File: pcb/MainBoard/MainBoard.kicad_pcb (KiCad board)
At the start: 4 copper layers, 50 x 50 mm, 133 parts, among them J101 Conn_02x05_Odd_Even, J301 USB_C_Receptacle_USB2.0, J501 Conn_01x01, J502 Conn_01x01, J503 Conn_01x01, J504 Conn_01x01, J505 Conn_01x01, J506 Conn_01x01, J507 Conn_01x01, J508 Conn_01x01, J509 Conn_01x01, J510 Conn_01x01, J511 Conn_01x01, J512 Conn_01x01, J513 Conn_01x01, J514 Conn_01x01, J515 Conn_01x01, J516 Conn_01x01, J517 Conn_01x01, J518 Conn_01x01, J519 Conn_01x01, J520 Conn_01x01, J801 AudioJack3_Ground, Q501 HL2304, U201 SHOU HAN TF PUSH, U401 RP2040, U402 W25Q128JVSIQ, U601 TJA1050T, U701 XC6206PxxxMR-Regulator_Linear, U702 INA180A1, X401 12MHz

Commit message: dump pcb
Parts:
- removed C406: 100nF, Capacitor_SMD:C_0402_1005Metric
- removed C704: 100u, Capacitor_Tantalum_SMD:CP_EIA-3528-15_AVX-H
- removed TP704: TestPoint, TestPoint:TestPoint_Pad_D1.0mm
- added C105: 22u, Capacitor_SMD:C_0805_2012Metric, F.Cu at (157.5, 34.7)
- added C106: 22u, Capacitor_SMD:C_0805_2012Metric, F.Cu at (160.6, 36.8)
- added C501: 22u, Capacitor_SMD:C_0805_2012Metric, F.Cu at (147.6, 33.5)
- added C502: 470u, Capacitor_SMD:CP_Elec_8x10.5, F.Cu at (123.7, 45.9)
- added C503: 100u, Capacitor_Tantalum_SMD:CP_EIA-3528-15_AVX-H, F.Cu at (126.2, 37.7)
- added C504: 22u, Capacitor_SMD:C_0805_2012Metric, F.Cu at (124.2, 55.1)
- added C505: 22u, Capacitor_SMD:C_0805_2012Metric, F.Cu at (137.0, 58.5)
- added C709: 4.7uF, Capacitor_SMD:C_0805_2012Metric, F.Cu at (142.3, 60.4)
- added C710: 4.7uF, Capacitor_SMD:C_0805_2012Metric, F.Cu at (139.6, 57.4)
- added C711: 4.7uF, Capacitor_SMD:C_0603_1608Metric, F.Cu at (147.0, 54.9)
- added C712: 4.7uF, Capacitor_SMD:C_0805_2012Metric, F.Cu at (139.6, 53.6)
- added C713: 100u, Capacitor_SMD:C_1206_3216Metric, F.Cu at (154.5, 52.6)
- added C714: 100pF, Capacitor_SMD:C_0402_1005Metric, F.Cu at (137.7, 66.5)
- added H501: JLCToolingHole, led-matrix:jlcpcb-tooling-hole, F.Cu at (167.5, 33.5)
- added H502: JLCToolingHole, led-matrix:jlcpcb-tooling-hole, F.Cu at (167.5, 81.0)
- added H503: JLCToolingHole, led-matrix:jlcpcb-tooling-hole, F.Cu at (120.0, 33.5)
- added H504: JLCToolingHole, led-matrix:jlcpcb-tooling-hole, F.Cu at (120.0, 81.0)
- added J102: Mechanical, Connector_PinHeader_2.54mm:PinHeader_1x02_P2.54mm_Vertical, F.Cu at (158.7, 69.8)
- added J103: Mechanical, Connector_PinHeader_2.54mm:PinHeader_1x02_P2.54mm_Vertical, F.Cu at (127.5, 34.2)
- added J104: Mechanical, Connector_PinHeader_2.54mm:PinHeader_1x02_P2.54mm_Vertical, F.Cu at (120.8, 73.5)
- added J105: DebugConn, Connector_PinSocket_2.54mm:PinSocket_1x05_P2.54mm_Horizontal, B.Cu at (158.6, 49.5)
- added J601: CANConn, Connector_JST:JST_EH_S2B-EH_1x02_P2.50mm_Horizontal, F.Cu at (157.5, 75.4)
- added JP101: SolderJumper_3_Open, led-matrix:SolderJumper-3_Open_RoundedPad_Smol, B.Cu at (159.7, 41.5)
- added JP102: SolderJumper_3_Open, led-matrix:SolderJumper-3_Open_RoundedPad_Smol, B.Cu at (159.8, 38.0)
- added JP103: SolderJumper_3_Open, led-matrix:SolderJumper-3_Open_RoundedPad_Smol, F.Cu at (148.4, 35.3)
- added JP104: SolderJumper_3_Open, led-matrix:SolderJumper-3_Open_RoundedPad_Smol, B.Cu at (134.6, 36.9)
- added JP504: SolderJumper_3_Open, led-matrix:SolderJumper-3_Open_RoundedPad_Smol, F.Cu at (162.2, 34.0)
- added JP505: SolderJumper_3_Open, led-matrix:SolderJumper-3_Open_RoundedPad_Smol, B.Cu at (125.4, 61.2)
- added JP506: SolderJumper_3_Open, led-matrix:SolderJumper-3_Open_RoundedPad_Smol, B.Cu at (132.2, 61.2)
- added JP507: SolderJumper_3_Open, led-matrix:SolderJumper-3_Open_RoundedPad_Smol, B.Cu at (128.5, 57.0)
- added JP508: SolderJumper_3_Open, led-matrix:SolderJumper-3_Open_RoundedPad_Smol, B.Cu at (128.4, 65.1)
- added JP509: SolderJumper_3_Open, led-matrix:SolderJumper-3_Open_RoundedPad_Smol, B.Cu at (129.5, 66.8)
- added JP601: SolderJumper_2_Open, led-matrix:SolderJumper-2_Open_RoundedPad_Smol, B.Cu at (156.2, 71.5)
- added JP701: SolderJumper_3_Open, led-matrix:SolderJumper-3_Open_RoundedPad_Smol, B.Cu at (139.5, 55.5)
- added Q502: HL2304, Package_TO_SOT_SMD:SOT-23, F.Cu at (128.8, 61.1)
- added Q503: HL2304, Package_TO_SOT_SMD:SOT-23, F.Cu at (125.4, 61.1)
- added Q504: HL2304, Package_TO_SOT_SMD:SOT-23, F.Cu at (132.2, 61.1)
- added Q505: HL2304, Package_TO_SOT_SMD:SOT-23, F.Cu at (127.2, 56.0)
- added Q506: HL2304, Package_TO_SOT_SMD:SOT-23, F.Cu at (126.1, 65.8)
- added Q507: HL2304, Package_TO_SOT_SMD:SOT-23, F.Cu at (130.9, 65.9)
- added R105: 2k2, Resistor_SMD:R_0402_1005Metric, F.Cu at (136.0, 39.1)
- added R106: 2k2, Resistor_SMD:R_0402_1005Metric, F.Cu at (137.1, 38.7)
- added R213: 47k, Resistor_SMD:R_0603_1608Metric, F.Cu at (147.1, 72.4)
- added R214: 47k, Resistor_SMD:R_0603_1608Metric, F.Cu at (145.6, 72.4)
- added R215: 47k, Resistor_SMD:R_0603_1608Metric, F.Cu at (144.1, 72.4)
- added R216: 47k, Resistor_SMD:R_0603_1608Metric, F.Cu at (142.6, 72.4)
- added R508: 4k7, Resistor_SMD:R_0402_1005Metric, F.Cu at (128.3, 58.7)
- added R509: 10k, Resistor_SMD:R_0402_1005Metric, F.Cu at (128.9, 63.5)
- added R510: 4k7, Resistor_SMD:R_0402_1005Metric, F.Cu at (131.7, 58.7)
- added R511: 10k, Resistor_SMD:R_0402_1005Metric, F.Cu at (132.2, 63.5)
- added R512: 4k7, Resistor_SMD:R_0402_1005Metric, F.Cu at (134.4, 56.6)
- added R513: 4k7, Resistor_SMD:R_0402_1005Metric, F.Cu at (123.7, 66.4)
- added R514: 10k, Resistor_SMD:R_0402_1005Metric, F.Cu at (128.5, 66.3)
- added R515: 4k7, Resistor_SMD:R_0402_1005Metric, F.Cu at (133.8, 65.9)
- added R602: 120R, Resistor_SMD:R_0402_1005Metric, F.Cu at (156.2, 71.5)
- added R705: 1k5, Resistor_SMD:R_0402_1005Metric, F.Cu at (139.0, 61.4)
- added R706: 470R, Resistor_SMD:R_0402_1005Metric, F.Cu at (145.0, 55.1)
- added R707: 1k, Resistor_SMD:R_0402_1005Metric, F.Cu at (145.0, 53.2)
- added R708: 1k8, Resistor_SMD:R_0402_1005Metric, F.Cu at (146.0, 53.2)
- added R709: 150R, Resistor_SMD:R_0402_1005Metric, F.Cu at (147.0, 53.2)
- added SW101: SW, Button_Switch_SMD:SW_SPST_B3U-3000P, F.Cu at (166.5, 56.2)
- added SW102: SW, Button_Switch_SMD:SW_SPST_B3U-3000P, F.Cu at (166.5, 51.2)
- added TP706: TestPoint, TestPoint:TestPoint_Pad_D1.0mm, B.Cu at (139.5, 57.9)
- added TP707: TestPoint, TestPoint:TestPoint_Pad_D1.0mm, B.Cu at (139.5, 53.1)
- added U703: XC6206PxxxMR-Regulator_Linear, Package_TO_SOT_SMD:SOT-23, F.Cu at (142.3, 57.4)
- added U704: CJ431, Package_TO_SOT_SMD:SOT-23, F.Cu at (142.5, 53.7)
- C101, C102, C103, C104: value C -> 1uf; footprint Capacitor_SMD:C_0603_1608Metric -> Capacitor_SMD:C_0402_1005Metric
- C703: value 4.7uF -> 22u
- C705: value 22uF -> 100u; footprint Capacitor_SMD:C_1206_3216Metric -> Capacitor_SMD:CP_Elec_6.3x7.7
- C706, C708: value 22uF -> 22u; footprint Capacitor_SMD:C_1206_3216Metric -> Capacitor_SMD:C_0805_2012Metric
- J101: value Conn_02x05_Odd_Even -> DaughterConn; footprint Connector_PinHeader_2.00mm:PinHeader_2x05_P2.00mm_Vertical -> Connector_PinHeader_2.54mm:PinHeader_2x05_P2.54mm_Vertical
- J501, J502, J503, J504, J505, J506, J507, J508, J509, J510, J511, J512, J513, J514, J515, J516, J517, J518, J519, J520, U201: moved to B.Cu
- JP501, JP502: value SolderJumper_2_Open -> SolderJumper_3_Open; footprint Jumper:SolderJumper-2_P1.3mm_Open_RoundedPad1.0x1.5mm -> led-matrix:SolderJumper-3_Open_RoundedPad_Smol; moved to B.Cu
- JP503: footprint Jumper:SolderJumper-3_P1.3mm_Open_RoundedPad1.0x1.5mm -> led-matrix:SolderJumper-3_Open_RoundedPad_Smol; moved to B.Cu
- Q501: footprint PCM_Package_TO_SOT_SMD_AKL:SOT-23 -> Package_TO_SOT_SMD:SOT-23
- R103, R104: value 100R -> 4k7
- R201, R202, R203, R204, R205, R206, R211, R212: value 10k -> 47k
- R207, R208, R209, R210: value 10k -> 33R; footprint Resistor_SMD:R_0603_1608Metric -> Resistor_SMD:R_0402_1005Metric
- R501, R507: value 10k -> 4k7
- U701: value XC6206PxxxMR-Regulator_Linear -> AMS1117-3.3; footprint Package_TO_SOT_SMD:SOT-23 -> Package_TO_SOT_SMD:SOT-223-3_TabPin2
- moved R601 141.3 mm to (152.3, 61.1), turned to 90 degrees
- moved R503 141.1 mm to (159.8, 34.5), turned to -90 degrees
- moved C601 139.6 mm to (153.3, 61.1), turned to 90 degrees
- moved U601 136.1 mm to (154.0, 65.8), turned to -90 degrees
- moved D601 136.0 mm to (158.0, 72.2)
- moved D602 133.9 mm to (154.5, 72.2), turned to 180 degrees
- moved R502 132.9 mm to (151.3, 35.0), turned to 180 degrees
- moved D501 131.1 mm to (164.8, 33.8)
- moved J510 128.3 mm to (163.5, 32.2)
- moved J509 128.2 mm to (161.2, 32.2)
- moved C706 126.1 mm to (147.2, 80.8), turned to 0 degrees
- moved C708 121.8 mm to (135.6, 80.8), turned to 180 degrees
- moved TP702 120.0 mm to (136.2, 75.8)
- moved C705 119.5 mm to (141.6, 78.4), turned to 0 degrees
- moved TP703 117.4 mm to (134.8, 72.4)
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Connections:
- net Net-(J301-SHIELD) renamed /usbc/USB_SHIELD
- C101 pad 1: /CC1 -> /CC1_F
- C102 pad 1: /CC2 -> /CC2_F
- C103 pad 1: GND -> /5v_sense_F
- C104 pad 1: /Isense -> /Isense_F
- C701 pad 1: /power/5V_FILTERED -> +5V
- C708 pad 1: +5V -> /power/VBUS
- D505 pad 1: /COL_SER -> /pads/COL_SER_OUT
- D506 pad 1: /COL_~{OE} -> /pads/COL_~{OE}_OUT
- D507 pad 1: /COL_RCLK -> /pads/COL_RCLK_OUT
- D508 pad 1: /COL_SRCLK -> /pads/COL_SRCLK_OUT
- D509 pad 1: /COL_~{SRCLR} -> /pads/COL_~{SRCLR}_OUT
- J101 pad 1: /GPIO15 -> +5V
- J101 pad 2: +5V -> +3V3
- J101 pad 3: /GPIO14 -> /GPIO15
- J101 pad 4: +3V3 -> /GPIO14
- J101 pad 6: /GPIO9 -> /GPIO12
- J101 pad 7: /GPIO12 -> /GPIO11
- J101 pad 9: /GPIO11 -> /GPIO9
- JP501 pad 1: /pads/COL_VCC -> +3V3
- JP501 pad 2: +3V3 -> /pads/COL_VCC
- JP502 pad 1: /pads/COL_VCC -> /COL_RCLK
- JP502 pad 2: +5V -> /pads/COL_RCLK_OUT
- JP503 pad 1: /COL_SER -> /pads/COL_SER_5V_BIDI
- JP503 pad 2: /pads/COL_SER_OUT -> Net-(JP503-C)
- Q501 pad 3: /pads/COL_SER_5V -> /pads/COL_SER_5V_BIDI
- R101 pad 2: Net-(R101-Pad2) -> /RESET_SW
- R102 pad 2: Net-(R102-Pad2) -> /CS_SW
- R202 pad 2: /SD_MISO -> /microsd/SD_MISO_DAT0
- R203 pad 2: /SD_SCLK -> /microsd/SD_CLK
- R204 pad 2: /SD_MOSI -> /microsd/SD_MOSI_CMD
- R205 pad 2: /SD_CS -> /microsd/SD_CS_DAT3
- R207 pad 1: /microsd/SD_DAT1 -> /SD_CS
- R207 pad 2: GND -> /microsd/SD_CS_DAT3
- R208 pad 1: /SD_MISO -> /SD_MOSI
- R208 pad 2: GND -> /microsd/SD_MOSI_CMD
- R209 pad 2: GND -> /microsd/SD_CLK
- R210 pad 1: /SD_MOSI -> /SD_MISO
- R210 pad 2: GND -> /microsd/SD_MISO_DAT0
- R211 pad 1: /SD_CS -> /microsd/SD_DAT1
- R212 pad 1: /microsd/SD_DAT2 -> /microsd/SD_MISO_DAT0
- R402 pad 1: /USB_D- -> /USB_D+
- R403 pad 1: /USB_D+ -> /USB_D-
- R501 pad 1: /pads/COL_VCC -> +5V
- R501 pad 2: /COL_~{OE} -> /pads/COL_~{OE}_5V
- R503 pad 1: /pads/ROW_VLED -> Net-(JP504-B)
- R504 pad 1: /COL_~{SRCLR} -> /COL_~{OE}
- R701 pad 2: GND -> /5V_sense
- U201 pad 2: /SD_CS -> /microsd/SD_CS_DAT3
- U201 pad 3: /SD_MOSI -> /microsd/SD_MOSI_CMD
- U201 pad 5: /SD_SCLK -> /microsd/SD_CLK
- U201 pad 7: /SD_MISO -> /microsd/SD_MISO_DAT0
- U401 pad 14: /GPIO13 -> /GPIO11
- U401 pad 16: /GPIO11 -> /GPIO13
- U401 pad 17: /ROW_SER -> /rp2040/GPIO14
- U401 pad 18: /ROW_~{SRCLR} -> /rp2040/GPIO15
- U401 pad 24: /rp2040/SWCLK -> /SWCLK
- U401 pad 25: /rp2040/SWD -> /SWD
- U401 pad 29: /ROW_~{OE} -> /ROW_SRCLK
- U401 pad 30: /ROW_RCLK -> /ROW_~{OE}
- U401 pad 31: /ROW_SRCLK -> /ROW_RCLK
- U401 pad 40: GND -> /5v_sense_F
- U401 pad 41: /Isense -> /Isense_F
- U401 pad 7: /CAN_TXD -> /CAN_RXD
- U401 pad 8: /CAN_RXD -> /CAN_S
- U401 pad 9: /CAN_S -> /CAN_TXD
- U701 pad 3: /power/5V_FILTERED -> +5V
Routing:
- net GND: track 0.00 -> 212.6 mm, vias 0 -> 217
- net +3V3: track 0.00 -> 188.9 mm, vias 0 -> 16
- net +5V: track 0.00 -> 176.2 mm, vias 0 -> 19
- net /COL_~{OE}: track 0.00 -> 59.2 mm, vias 0 -> 2
- net /COL_~{SRCLR}: track 0.00 -> 57.1 mm, vias 0 -> 4
- net /COL_RCLK: track 0.00 -> 54.6 mm, vias 0 -> 2
- net /COL_SRCLK: track 0.00 -> 50.5 mm, vias 0 -> 2
- net /COL_SER: track 0.00 -> 50.5 mm, vias 0 -> 2
- net /CC1: track 0.00 -> 47.1 mm, vias 0 -> 2
- net /microsd/SD_CS_DAT3: track 0.00 -> 45.0 mm, vias 0 -> 4
- net /microsd/SD_CLK: track 0.00 -> 44.8 mm, vias 0 -> 2
- net /CC2: track 0.00 -> 42.0 mm, vias 0 -> 2
- net /microsd/SD_MOSI_CMD: track 0.00 -> 41.9 mm, vias 0 -> 2
- net /USB_D+: track 0.00 -> 41.6 mm, vias 0 -> 2
- net /USB_D-: track 0.00 -> 38.3 mm, vias 0 -> 2
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- added copper zone on B.Cu, net +3V3
- added copper zone on B.Cu, net +5V
- added copper zone on F.Cu, net +5V
- added copper zone on In1.Cu, net +5V
- added copper zone on F.Cu, net /power/5V_FILTERED
- added copper zone on In1.Cu, net /power/5V_FILTERED
- added copper zone on F.Cu, net /power/VBUS
- added copper zone on B.Cu, net /usbc/USB_SHIELD
- added copper zone on B.Cu, net GND
- added copper zone on F.Cu, net GND
- added copper zone on In1.Cu, net GND
- added copper zone on In2.Cu, net GND
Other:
- board text added: "(le bodge)"
- board text added: "10"
- board text added: "11"
- board text added: "12"
- board text added: "120Ω termination"
- board text added: "13"
- board text added: "14·"
- board text added: "15·"
- board text added: "2024"
- board text added: "3V3"
- board text added: "5V"
- board text added: "5V_F"
- board text added: "9"
- board text added: "AUDIO"
- board text added: "B"
- board text added: "BOOT"
- board text added: "CAN"
- board text added: "COL|SEP."
- board text added: "DEBUG"
- board text added: "GND"
- board text added: "GPIO"
- board text added: "GPIO|SER"
- board text added: "GPIO|~{SRCLR}"
- board text added: "HSWAW"
- board text added: "JLCJLCJLCJLC"
- board text added: "PIN 14"
- board text added: "PIN 15"
- board text added: "R"
- board text added: "RCLK"
- board text added: "RESET"
- board text added: "RX"
- board text added: "Reg."
- board text added: "Rev A"
- board text added: "SEP.|COL"
- board text added: "SER"
- board text added: "SRCLK"
- board text added: "SWC"
- board text added: "SWCLK"
- board text added: "SWD"
- board text added: "Shunt"
- board text added: "TX"
- board text added: "USB"
- board text added: "VBUS"
- board text added: "VCC"
- board text added: "VLED"
- board text added: "Vref"
- board text added: "bidi"
- board text added: "by radex"
- board text added: "column driver level shifting"
- board text added: "le bodge"
- board text added: "main board"
- board text added: "matri"
- board text added: "microSD"
- board text added: "rad"
- board text added: "radex"
- board text added: "x"
- board text added: "~{OE}"
- board text added: "~{SRCLR}"
- board text added: "·14"
- board text added: "·15"

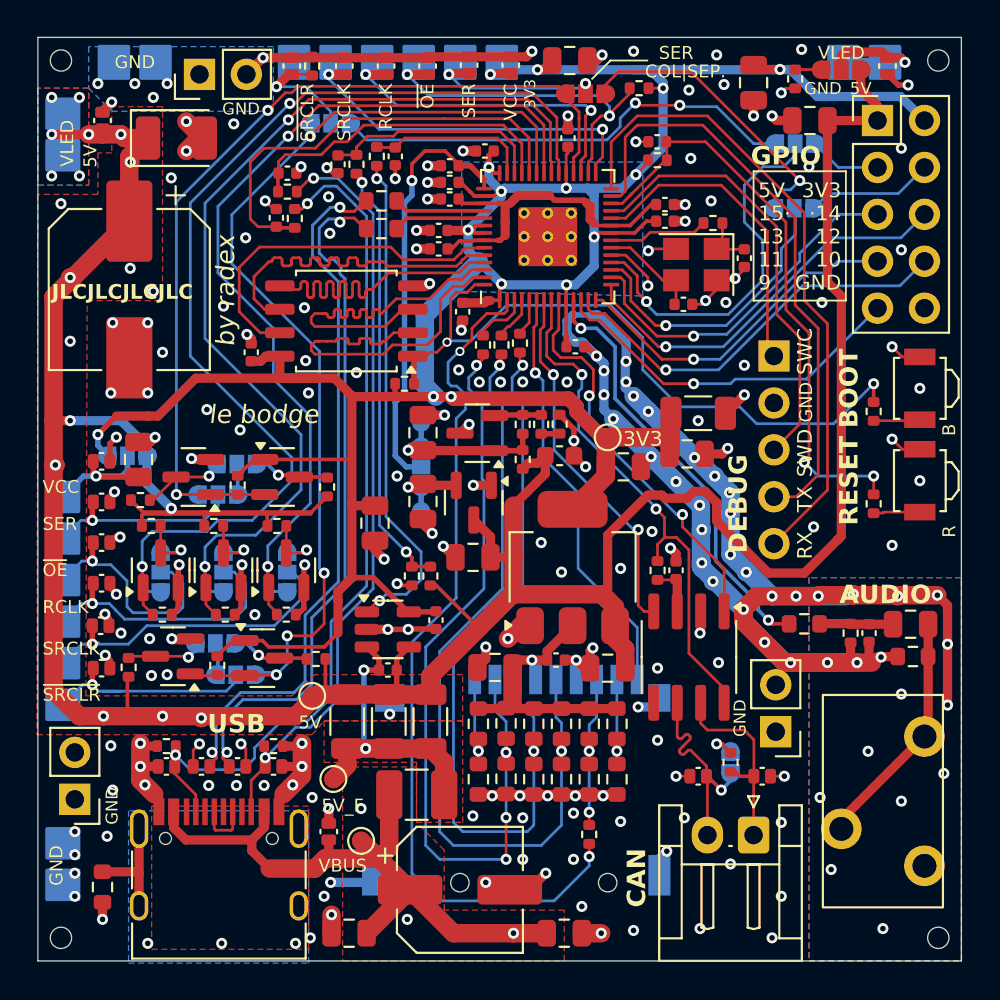
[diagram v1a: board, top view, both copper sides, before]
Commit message: MainBoard: fixes, simplify, BOM optimize, DRC fixes, ERC fixes
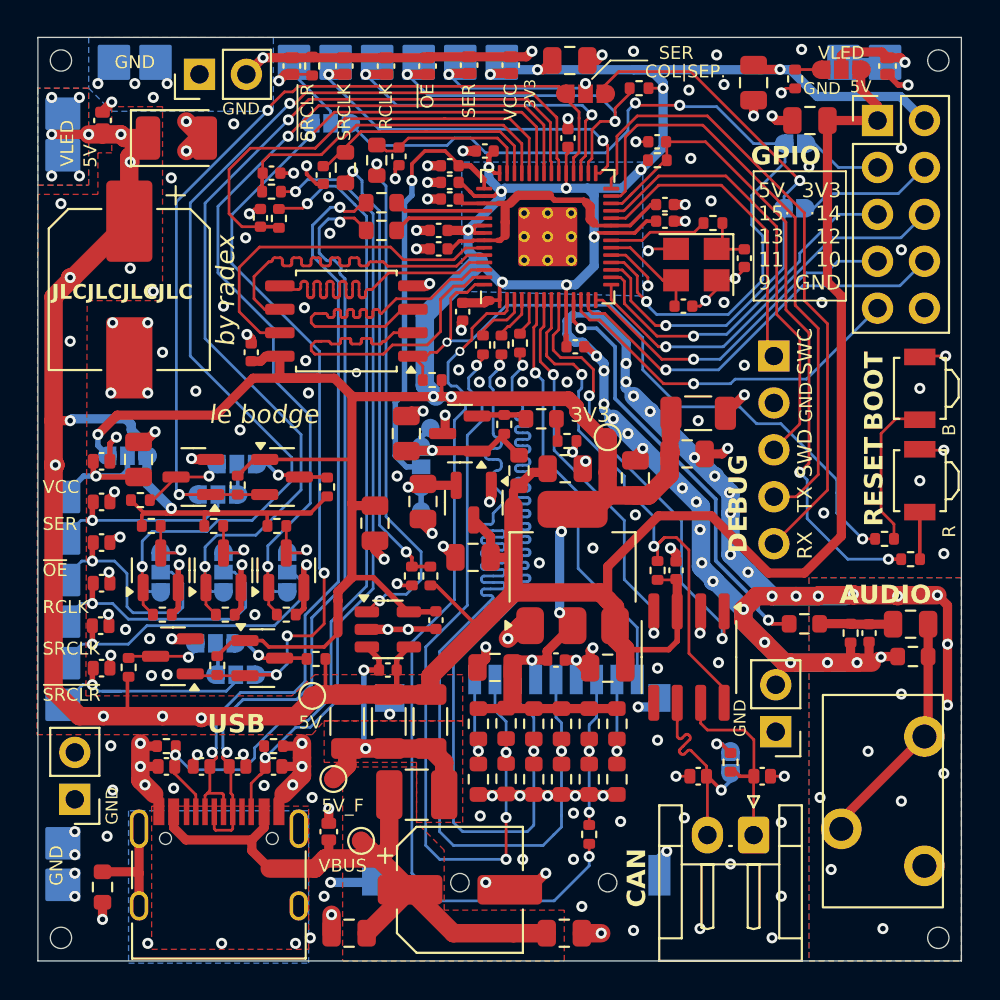
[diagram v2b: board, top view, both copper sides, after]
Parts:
- C101, C102, C103, C104: value 1uf -> 1u
- C401, C402, C403, C404, C405, C407, C408, C409, C410, C416, C707: value 100nF -> 100n
- C411, C412, C413: value 1uF -> 1u
- C414, C415: value 33pF -> 33p
- C701, C702, C709, C710, C712: value 4.7uF -> 4u7
- C711: value 4.7uF -> 4u7; footprint Capacitor_SMD:C_0603_1608Metric -> Capacitor_SMD:C_0805_2012Metric
- C714: value 100pF -> 100p
- JP101, JP102: value SolderJumper_3_Open -> SolderJumper_2_Open; footprint led-matrix:SolderJumper-3_Open_RoundedPad_Smol -> led-matrix:SolderJumper-2_Open_RoundedPad_Smol
- R103, R104, R501, R507, R508, R510, R512, R513, R515: value 4k7 -> 5k1
- R105, R106: value 2k2 -> 1k8; footprint Resistor_SMD:R_0402_1005Metric -> Resistor_SMD:R_0603_1608Metric
- R706, R708: footprint Resistor_SMD:R_0402_1005Metric -> Resistor_SMD:R_0603_1608Metric
- R709: value 150R -> 120R
- moved R102 6.93 mm to (164.6, 59.4), turned to 0 degrees
- moved R101 3.61 mm to (166.0, 60.5), turned to 0 degrees
- moved R405 1.51 mm to (140.1, 50.8), turned to 180 degrees
- moved R707 1.00 mm to (144.0, 53.2)
- moved R709 0.99 mm to (147.4, 54.1), turned to 0 degrees
- moved C103 0.99 mm to (134.2, 39.7)
- moved U704 0.94 mm to (141.6, 53.7)
- moved C712 0.90 mm to (138.7, 53.7)
- moved C702 0.88 mm to (151.1, 56.1), turned to 90 degrees
- moved C101 0.86 mm to (130.8, 42.0)
- moved C102 0.86 mm to (131.4, 39.6)
- moved R103 0.86 mm to (131.8, 42.0)
- moved R104 0.86 mm to (131.4, 40.6)
- moved C711 0.76 mm to (147.3, 55.6)
- moved R706 0.63 mm to (144.8, 55.7)
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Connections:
- JP101 pad 2: /rp2040/GPIO14 -> /GPIO14
- JP102 pad 2: /rp2040/GPIO15 -> /GPIO15
- U401 pad 17: /rp2040/GPIO14 -> /ROW_SER_J
- U401 pad 18: /rp2040/GPIO15 -> /ROW_~{SRCLR}_J
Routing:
- net /ROW_~{SRCLR}_J: track 25.4 -> 45.8 mm, vias 2 -> 3
- net /rp2040/GPIO15: track 20.3 -> 0.00 mm, vias 1 -> 0
- net /microsd/SD_MOSI_CMD: track 41.9 -> 59.1 mm
- net /rp2040/GPIO14: track 16.2 -> 0.00 mm, vias 1 -> 0
- net /ROW_SER_J: track 16.1 -> 31.4 mm, vias 1 -> 2
- net /microsd/SD_CLK: track 44.8 -> 59.0 mm
- net +3V3: track 188.9 -> 197.1 mm, vias 16 -> 18
- net /CS_SW: track 2.27 -> 8.51 mm
- net /USB_D-: track 38.3 -> 42.6 mm
- net /~{RESET}: track 32.1 -> 36.2 mm
- net GND: track 212.6 -> 209.3 mm, vias 217 -> 215
- net /CAN_TXD: track 21.8 -> 24.6 mm
- net /USB_D+: track 41.6 -> 44.3 mm
- net /CS: track 37.8 -> 39.7 mm
- net /CAN_RXD: track 19.9 -> 21.8 mm
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
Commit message: some pcb review
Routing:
- net +3V3: track 197.1 -> 201.6 mm, vias 18 -> 20
- net /power/5V_FILTERED: vias 2 -> 4

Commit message: pcb: fixes, improvements
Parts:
- removed C709, C710: 4u7, Capacitor_SMD:C_0805_2012Metric
- removed TP706: TestPoint, TestPoint:TestPoint_Pad_D1.0mm
- removed U703: XC6206PxxxMR-Regulator_Linear, Package_TO_SOT_SMD:SOT-23
- added C418: 22u, Capacitor_SMD:C_0805_2012Metric, F.Cu at (131.8, 52.5)
- added D701: LED, Diode_SMD:D_0603_1608Metric, F.Cu at (139.3, 56.5)
- added D702: LED, Diode_SMD:D_0603_1608Metric, F.Cu at (142.5, 56.5)
- added R710: 470R, Resistor_SMD:R_0603_1608Metric, F.Cu at (142.4, 60.1)
- added R711: 5k1, Resistor_SMD:R_0402_1005Metric, F.Cu at (137.2, 53.7)
- added R712: 2k, Resistor_SMD:R_0402_1005Metric, F.Cu at (145.8, 52.8)
- J601: footprint Connector_JST:JST_EH_S2B-EH_1x02_P2.50mm_Horizontal -> Connector_PinHeader_2.54mm:PinHeader_1x02_P2.54mm_Horizontal
- R201, R202, R203, R204, R205, R206, R211, R212, R213, R214, R215, R216: value 47k -> 10k
- R707: value 1k -> 680R
- R708: value 1k8 -> 680R; footprint Resistor_SMD:R_0603_1608Metric -> Resistor_SMD:R_0402_1005Metric
- R709: value 120R -> 2k
- R801: value 470R -> 220R
- moved R708 8.27 mm to (140.2, 58.8)
- moved R709 6.94 mm to (142.3, 58.8)
- moved J601 3.16 mm to (158.1, 72.3), turned to -90 degrees
- moved D601 2.75 mm to (155.8, 70.5), turned to 180 degrees
- moved R602 2.61 mm to (153.8, 70.6), turned to 90 degrees
- moved JP601 2.51 mm to (153.8, 71.0), turned to -90 degrees
- moved D602 1.80 mm to (152.7, 72.2)
- moved C505 0.45 mm to (137.0, 59.0)
- moved R707 0.20 mm to (144.2, 53.2)
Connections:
- JP701 pad 3: /power/VREF_REG -> +3V3
- R708 pad 1: /power/VREF_REF -> GND
- R708 pad 2: Net-(R708-Pad2) -> Net-(D701-Pad1)
- R709 pad 1: Net-(R708-Pad2) -> Net-(D702-Pad1)
- R709 pad 2: GND -> Net-(R709-Pad2)
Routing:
- net +3V3: track 201.6 -> 209.3 mm, vias 20 -> 21
- net /power/VREF_REG: track 4.77 -> 0.00 mm, vias 1 -> 0
- net /can/CANL: track 11.8 -> 8.15 mm
- net /can/CANH: track 10.9 -> 7.31 mm
- net /power/5V_FILTERED: track 16.9 -> 20.2 mm
- net Net-(D701-Pad1): track 0.00 -> 2.56 mm
- net GND: track 209.3 -> 211.7 mm, vias 215 -> 213
- net Net-(D702-Pad1): track 0.00 -> 2.33 mm
- net +5V: track 177.9 -> 175.6 mm
- net /power/VREF_SHUNT: track 10.6 -> 12.4 mm
- net Net-(R709-Pad2): track 0.00 -> 1.47 mm
- net Net-(R708-Pad2): track 1.23 -> 0.00 mm
- net /can/CAN_T_R: track 1.89 -> 1.13 mm
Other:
- board text added: "CANH"
- board text added: "CANL"

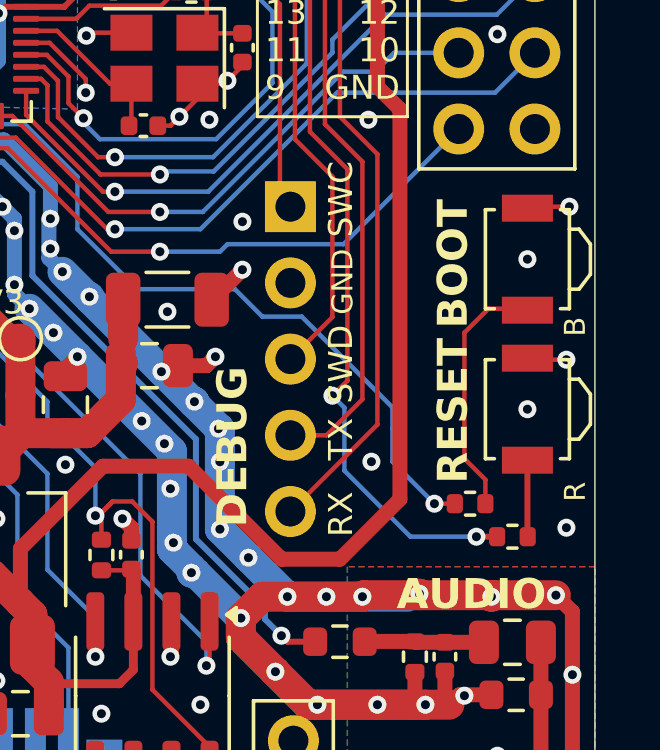
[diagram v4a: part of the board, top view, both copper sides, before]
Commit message: pcb: add microswitches
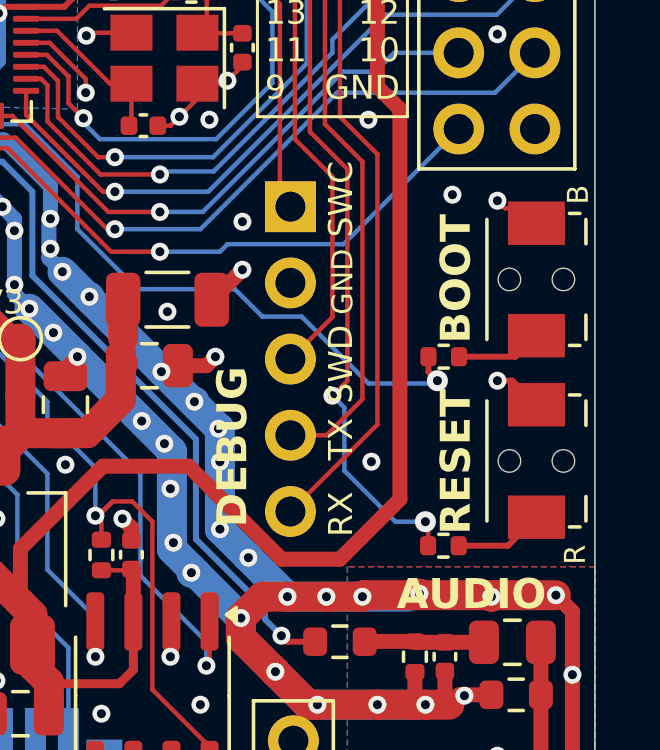
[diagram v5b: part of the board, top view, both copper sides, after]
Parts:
- SW101, SW102: footprint Button_Switch_SMD:SW_SPST_B3U-3000P -> led-matrix:HY-C-03
- moved R102 4.98 mm to (163.7, 54.5)
- moved R101 2.32 mm to (163.7, 60.8)
- moved SW101 1.75 mm to (166.8, 58.0)
- moved SW102 0.74 mm to (166.8, 51.9)
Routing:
- net /CS_SW: track 8.51 -> 2.87 mm
- net /CS: track 39.7 -> 37.3 mm
- net /~{RESET}: track 36.2 -> 34.5 mm
- net GND: vias 213 -> 211
